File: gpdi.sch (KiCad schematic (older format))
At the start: 13 parts, among them U1 LFE5U-85F-6BG381C

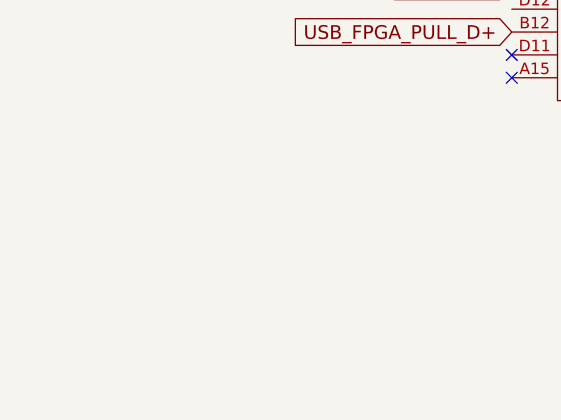
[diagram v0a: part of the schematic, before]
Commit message: Rewiering LCD OUT to bottom left
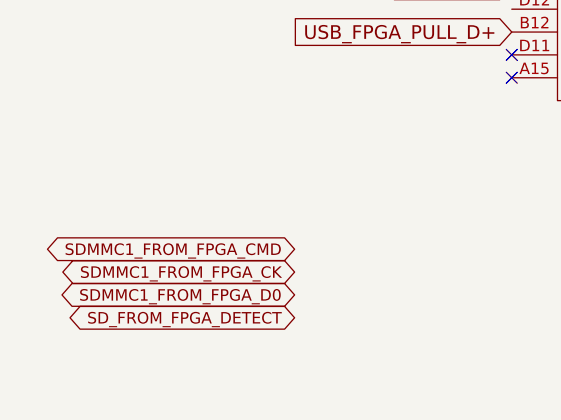
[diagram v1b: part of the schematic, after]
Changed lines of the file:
@@
 NoConn ~ 2850 3800
 NoConn ~ 4350 3700
+Text GLabel 1900 4850 0    50   BiDi ~ 0
+SD_FROM_FPGA_DETECT
+Text GLabel 1900 4550 0    50   BiDi ~ 0
+SDMMC1_FROM_FPGA_CMD
+Text GLabel 1900 4750 0    50   BiDi ~ 0
+SDMMC1_FROM_FPGA_D0
+Text GLabel 1900 4650 0    50   BiDi ~ 0
+SDMMC1_FROM_FPGA_CK
 $EndSCHEMATC

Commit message: Adding all SPI to FPGA resorting LCD TO FPGA
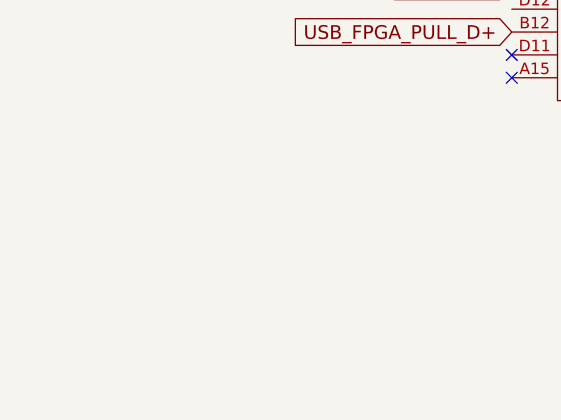
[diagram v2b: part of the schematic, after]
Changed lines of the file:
@@
 NoConn ~ 2850 3800
 NoConn ~ 4350 3700
-Text GLabel 1900 4850 0    50   BiDi ~ 0
-SD_FROM_FPGA_DETECT
-Text GLabel 1900 4550 0    50   BiDi ~ 0
-SDMMC1_FROM_FPGA_CMD
-Text GLabel 1900 4750 0    50   BiDi ~ 0
-SDMMC1_FROM_FPGA_D0
-Text GLabel 1900 4650 0    50   BiDi ~ 0
-SDMMC1_FROM_FPGA_CK
 $EndSCHEMATC
